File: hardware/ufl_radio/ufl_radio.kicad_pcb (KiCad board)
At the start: 6 copper layers, 46.8 x 62 mm, 142 parts, among them J2 U.FL, J3 Shield, J4 Shield, J5 U.FL, J6 Shield, J7 U.FL, J8 Shield, J9 U.FL, U1 MAX2769B, U2 CS48520S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

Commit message: Nearly ready
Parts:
- moved C37 14.7 mm to (175.8, 93.5)
- moved C42 14.7 mm to (188.8, 85.0)
- moved C22 10.3 mm to (188.8, 115.5), turned to 90 degrees
- moved C48 10.3 mm to (178.6, 86.8), turned to -90 degrees
- moved C16 8.96 mm to (178.6, 117.2), turned to -90 degrees
- moved C51 8.96 mm to (179.0, 77.8), turned to 0 degrees
- moved C39 8.73 mm to (184.2, 95.5), turned to 0 degrees
- moved C24 8.02 mm to (179.6, 117.2), turned to -90 degrees
- moved C54 7.33 mm to (184.2, 109.8), turned to 0 degrees
- moved C57 7.33 mm to (188.8, 100.3), turned to 90 degrees
- moved C18 5.45 mm to (179.0, 108.3)
- moved C27 5.31 mm to (184.0, 114.3), turned to 0 degrees
- moved C40 5.31 mm to (179.6, 86.8), turned to -90 degrees
- moved C49 5.31 mm to (184.0, 83.8), turned to 0 degrees
- moved C28 4.61 mm to (184.2, 94.5)
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
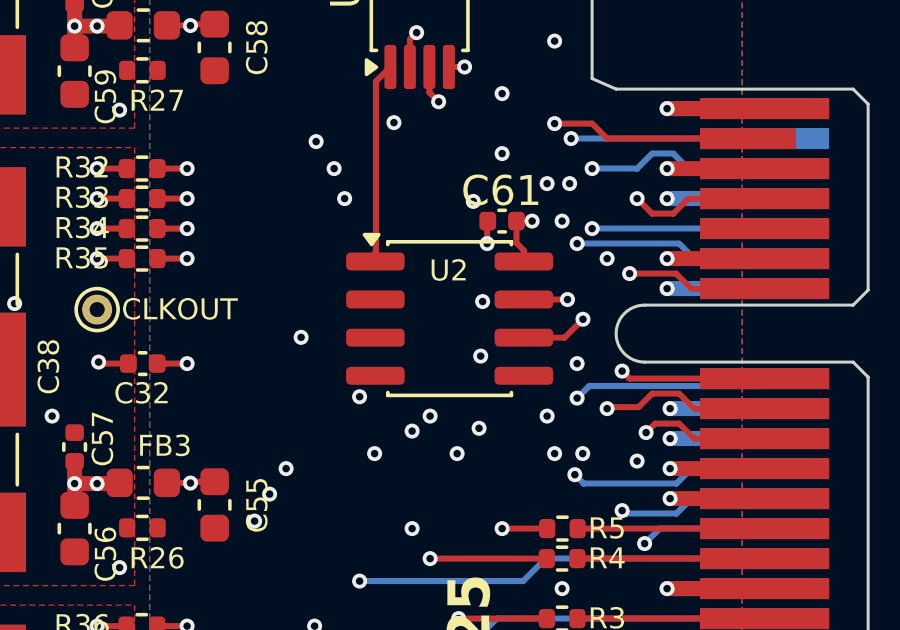
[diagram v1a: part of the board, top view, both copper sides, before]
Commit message: Replace the RS485 driver as it is no longer in production
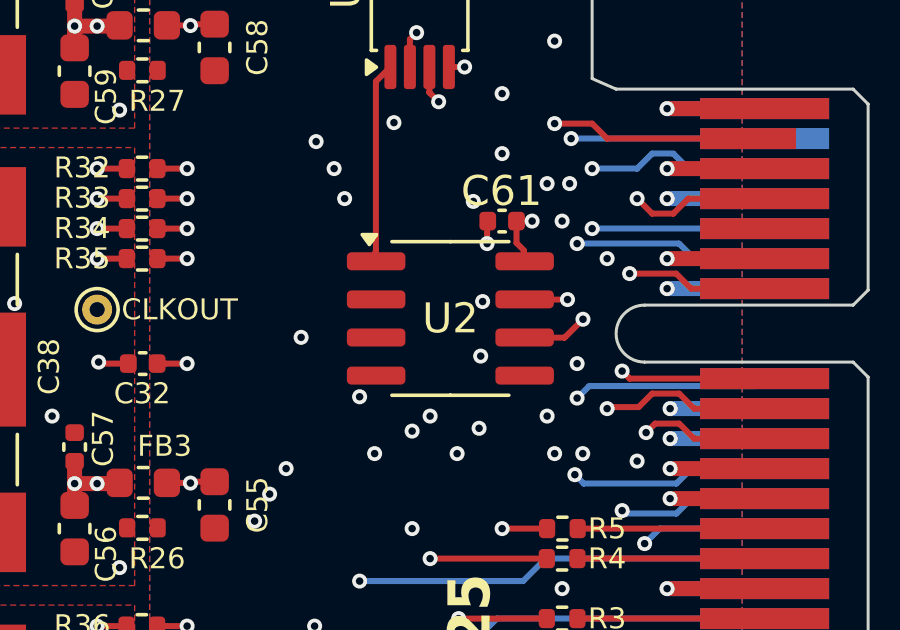
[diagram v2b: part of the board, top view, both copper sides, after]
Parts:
- U2: value CS48520S -> CS48520AS

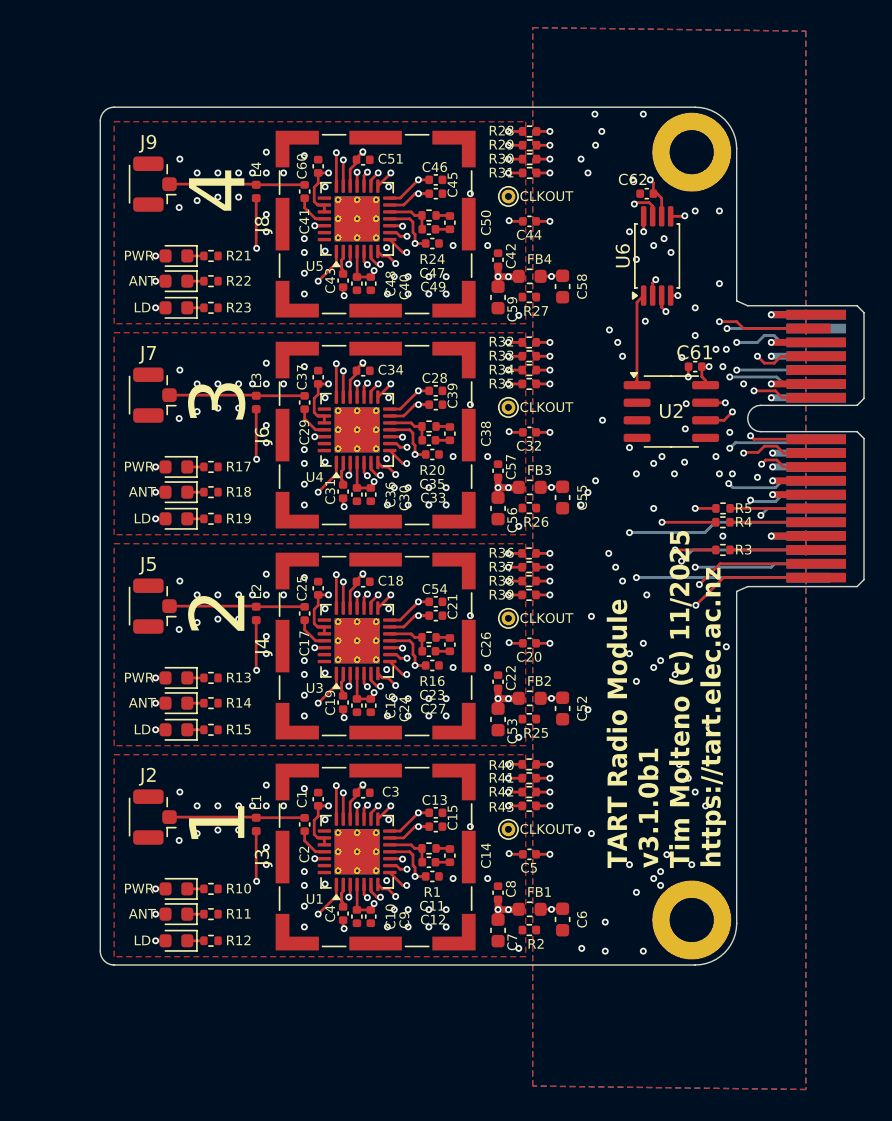
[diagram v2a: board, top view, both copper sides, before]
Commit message: Add a better panelize script and get the impedance right
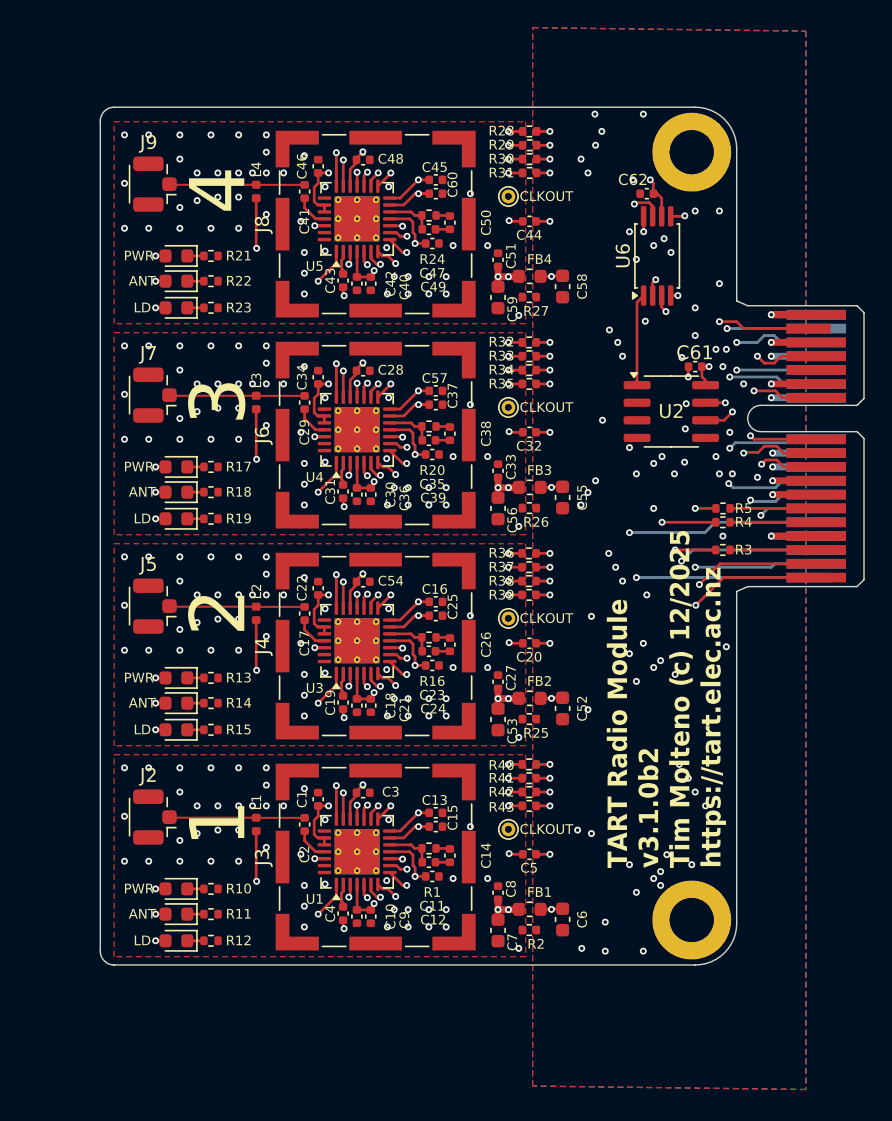
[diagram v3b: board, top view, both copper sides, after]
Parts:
- moved C22 14.7 mm to (175.8, 108.8)
- moved C51 12.1 mm to (188.8, 85.0), turned to 90 degrees
- moved C42 10.3 mm to (178.6, 86.8), turned to -90 degrees
- moved C16 9.42 mm to (184.2, 109.8), turned to 0 degrees
- moved C18 8.96 mm to (178.6, 117.2), turned to -90 degrees
- moved C48 8.96 mm to (179.0, 77.8), turned to 0 degrees
- moved C25 8.73 mm to (184.2, 110.8), turned to 0 degrees
- moved C37 8.73 mm to (184.2, 95.5), turned to 0 degrees
- moved C60 8.73 mm to (184.2, 80.2), turned to 0 degrees
- moved C46 8.56 mm to (175.8, 78.3), turned to 90 degrees
- moved C21 8.02 mm to (179.6, 117.2), turned to -90 degrees
- moved C57 7.33 mm to (184.2, 94.5), turned to 0 degrees
- moved C28 5.45 mm to (179.0, 93.0)
- moved C54 5.45 mm to (179.0, 108.3)
- moved C24 5.31 mm to (184.0, 114.3), turned to 0 degrees
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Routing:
- net /Radio4/AGND_local: vias 35 -> 46
- net /Radio3/AGND_local: vias 35 -> 46
- net /Radio2/AGND_local: vias 35 -> 46
- net /Radio1/AGND_local: vias 35 -> 46
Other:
- board text added: "TART Radio Module v3.1.0b2 Tim Molteno (c) 12/2025 https://tart.elec.ac.nz"
- board text added: "TART Radio Telescope Radio Module v3.1.0b2 Tim Molteno (c) 12/2025 https://tart.elec.ac.nz"
- board text removed: "TART Radio Module v3.1.0b1 Tim Molteno (c) 11/2025 https://tart.elec.ac.nz"
- board text removed: "TART Radio Telescope Radio Module v3.1.0b1 Tim Molteno (c) 11/2025 https://tart.elec.ac.nz"

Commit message: Fix up ground rules
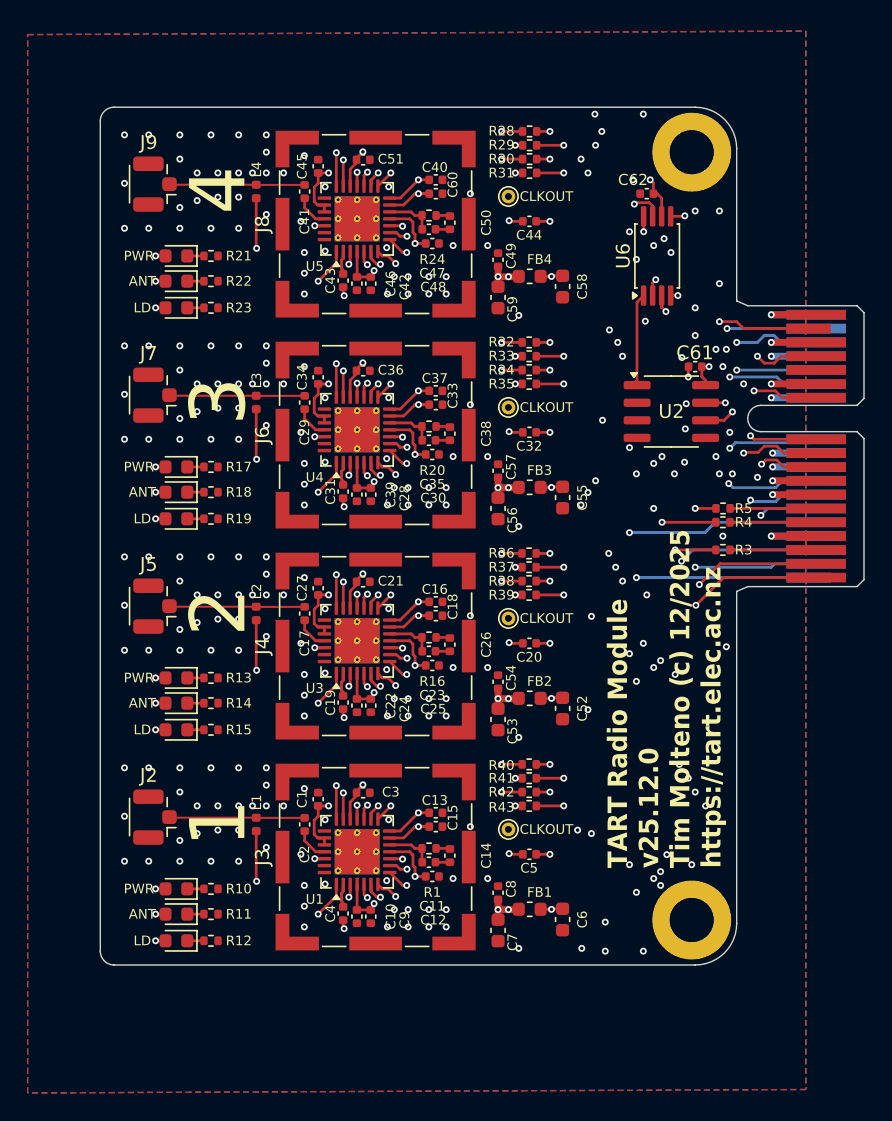
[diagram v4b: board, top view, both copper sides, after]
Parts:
- removed R2, R25, R26, R27: 0, Resistor_SMD:R_0402_1005Metric
- moved C27 14.7 mm to (175.8, 108.8)
- moved C51 12.1 mm to (179.0, 77.8), turned to 0 degrees
- moved C54 12.1 mm to (188.8, 115.5), turned to 90 degrees
- moved C21 8.97 mm to (179.0, 108.3), turned to 0 degrees
- moved C28 8.97 mm to (179.6, 102.0), turned to -90 degrees
- moved C36 8.97 mm to (179.0, 93.0), turned to 0 degrees
- moved C22 8.93 mm to (178.6, 117.2), turned to -90 degrees
- moved C46 8.93 mm to (178.6, 86.8), turned to -90 degrees
- moved C40 8.85 mm to (184.2, 79.2), turned to 0 degrees
- moved C18 8.65 mm to (184.2, 110.8), turned to 0 degrees
- moved C45 8.56 mm to (175.8, 78.3), turned to 90 degrees
- moved C48 7.85 mm to (184.0, 83.8)
- moved C57 7.33 mm to (188.8, 100.3), turned to 90 degrees
- moved C33 6.56 mm to (184.2, 95.5), turned to 0 degrees
- moved C30 6.17 mm to (184.0, 99.1), turned to 0 degrees
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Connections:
- C1 pad 2: /Radio1/AGND_local -> GNDREF
- C10 pad 2: /Radio1/AGND_local -> GNDREF
- C11 pad 1: /Radio1/AGND_local -> GNDREF
- C12 pad 2: /Radio1/AGND_local -> GNDREF
- C13 pad 2: /Radio1/AGND_local -> GNDREF
- C14 pad 2: /Radio1/AGND_local -> GNDREF
- C15 pad 2: /Radio1/AGND_local -> GNDREF
- C16 pad 2: /Radio2/AGND_local -> GNDREF
- C18 pad 2: /Radio2/AGND_local -> GNDREF
- C21 pad 2: /Radio2/AGND_local -> GNDREF
- C22 pad 2: /Radio2/AGND_local -> GNDREF
- C23 pad 1: /Radio2/AGND_local -> GNDREF
- C24 pad 2: /Radio2/AGND_local -> GNDREF
- C25 pad 2: /Radio2/AGND_local -> GNDREF
- C26 pad 2: /Radio2/AGND_local -> GNDREF
- C27 pad 2: /Radio2/AGND_local -> GNDREF
- C28 pad 2: /Radio3/AGND_local -> GNDREF
- C3 pad 2: /Radio1/AGND_local -> GNDREF
- C30 pad 2: /Radio3/AGND_local -> GNDREF
- C33 pad 2: /Radio3/AGND_local -> GNDREF
- C34 pad 2: /Radio3/AGND_local -> GNDREF
- C35 pad 1: /Radio3/AGND_local -> GNDREF
- C36 pad 2: /Radio3/AGND_local -> GNDREF
- C37 pad 2: /Radio3/AGND_local -> GNDREF
- C38 pad 2: /Radio3/AGND_local -> GNDREF
- C39 pad 2: /Radio3/AGND_local -> GNDREF
- C40 pad 2: /Radio4/AGND_local -> GNDREF
- C42 pad 2: /Radio4/AGND_local -> GNDREF
- C45 pad 2: /Radio4/AGND_local -> GNDREF
- C46 pad 2: /Radio4/AGND_local -> GNDREF
- C47 pad 1: /Radio4/AGND_local -> GNDREF
- C48 pad 2: /Radio4/AGND_local -> GNDREF
- C49 pad 2: /Radio4/AGND_local -> GNDREF
- C50 pad 2: /Radio4/AGND_local -> GNDREF
- C51 pad 2: /Radio4/AGND_local -> GNDREF
- C53 pad 2: /Radio2/AGND_local -> GNDREF
- C54 pad 2: /Radio2/AGND_local -> GNDREF
- C56 pad 2: /Radio3/AGND_local -> GNDREF
- C57 pad 2: /Radio3/AGND_local -> GNDREF
- C59 pad 2: /Radio4/AGND_local -> GNDREF
- C60 pad 2: /Radio4/AGND_local -> GNDREF
- C7 pad 2: /Radio1/AGND_local -> GNDREF
- C8 pad 2: /Radio1/AGND_local -> GNDREF
- C9 pad 2: /Radio1/AGND_local -> GNDREF
- J2 pad 2: /Radio1/AGND_local -> GNDREF
- J3 pad 1: /Radio1/AGND_local -> GNDREF
- J4 pad 1: /Radio2/AGND_local -> GNDREF
- J5 pad 2: /Radio2/AGND_local -> GNDREF
- J6 pad 1: /Radio3/AGND_local -> GNDREF
- J7 pad 2: /Radio3/AGND_local -> GNDREF
- J8 pad 1: /Radio4/AGND_local -> GNDREF
- J9 pad 2: /Radio4/AGND_local -> GNDREF
- R10 pad 2: /Radio1/AGND_local -> GNDREF
- R11 pad 2: /Radio1/AGND_local -> GNDREF
- R12 pad 2: /Radio1/AGND_local -> GNDREF
- R13 pad 2: /Radio2/AGND_local -> GNDREF
- R14 pad 2: /Radio2/AGND_local -> GNDREF
- R15 pad 2: /Radio2/AGND_local -> GNDREF
- R17 pad 2: /Radio3/AGND_local -> GNDREF
- R18 pad 2: /Radio3/AGND_local -> GNDREF
- R19 pad 2: /Radio3/AGND_local -> GNDREF
- R21 pad 2: /Radio4/AGND_local -> GNDREF
- R22 pad 2: /Radio4/AGND_local -> GNDREF
- R23 pad 2: /Radio4/AGND_local -> GNDREF
- U1 pad 29: /Radio1/AGND_local -> GNDREF
- U3 pad 29: /Radio2/AGND_local -> GNDREF
- U4 pad 29: /Radio3/AGND_local -> GNDREF
- U5 pad 29: /Radio4/AGND_local -> GNDREF
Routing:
- net GNDREF: track 30.4 -> 34.6 mm, vias 35 -> 219
- net /Radio4/AGND_local: track 1.04 -> 0.00 mm, vias 46 -> 0
- net /Radio3/AGND_local: track 1.04 -> 0.00 mm, vias 46 -> 0
- net /Radio2/AGND_local: track 1.04 -> 0.00 mm, vias 46 -> 0
- net /Radio1/AGND_local: track 1.04 -> 0.00 mm, vias 46 -> 0
- added copper zone on In2.Cu, net GNDREF
- added copper zone on In4.Cu, net GNDREF
- removed copper zone on F.Cu, net /Radio1/AGND_local
- removed copper zone on In1.Cu, net /Radio1/AGND_local
- removed copper zone on F.Cu, net /Radio2/AGND_local
- removed copper zone on In1.Cu, net /Radio2/AGND_local
- removed copper zone on F.Cu, net /Radio3/AGND_local
- removed copper zone on In1.Cu, net /Radio3/AGND_local
- removed copper zone on F.Cu, net /Radio4/AGND_local
- removed copper zone on In1.Cu, net /Radio4/AGND_local
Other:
- board text added: "TART Radio Module v25.12.0 Tim Molteno (c) 12/2025 https://tart.elec.ac.nz"
- board text removed: "TART Radio Module v3.1.0b2 Tim Molteno (c) 12/2025 https://tart.elec.ac.nz"

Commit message: Update and improve noise on ufl radio
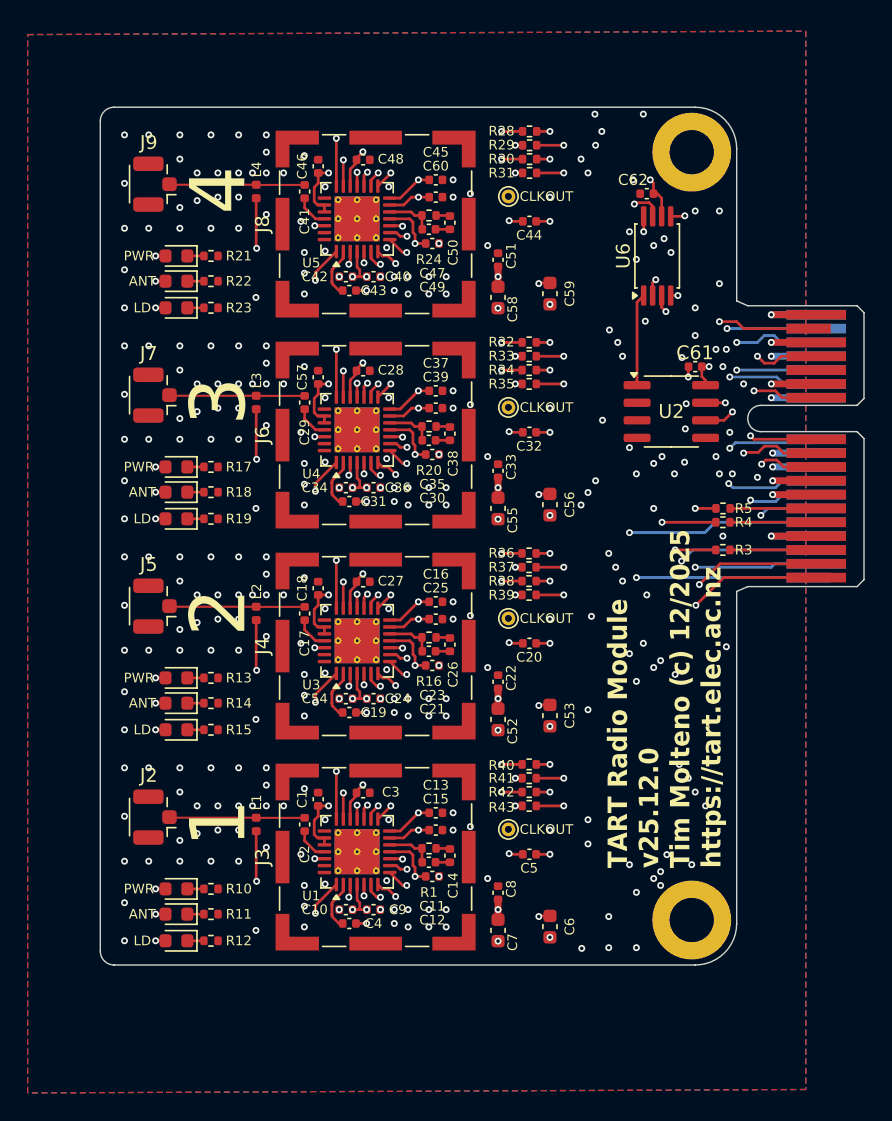
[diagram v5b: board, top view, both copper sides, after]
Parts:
- removed FB1, FB2, FB3, FB4: GZ1608D601TF, Inductor_SMD:L_0603_1608Metric
- moved C57 14.7 mm to (175.8, 93.5)
- moved C51 12.1 mm to (188.8, 85.0), turned to 90 degrees
- moved C54 11.1 mm to (177.8, 116.8), turned to 180 degrees
- moved C22 10.3 mm to (188.8, 115.5), turned to 90 degrees
- moved C28 8.97 mm to (179.0, 93.0), turned to 0 degrees
- moved C46 8.93 mm to (175.8, 78.3), turned to 90 degrees
- moved C18 8.73 mm to (175.8, 108.8), turned to 90 degrees
- moved C45 8.56 mm to (184.2, 79.2), turned to 0 degrees
- moved C36 8.48 mm to (179.8, 101.5)
- moved C39 8.46 mm to (184.2, 95.8), turned to 0 degrees
- moved C40 8.32 mm to (179.8, 86.2)
- moved C34 8.23 mm to (177.8, 101.5), turned to 180 degrees
- moved C21 7.85 mm to (184.0, 114.3)
- moved C48 7.85 mm to (179.0, 77.8)
- moved C33 6.56 mm to (188.8, 100.3), turned to 90 degrees
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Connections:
- C1 pad 1: /Radio1/3v3_local -> VCC
- C10 pad 1: /Radio1/3v3_local -> VCC
- C12 pad 1: /Radio1/3v3_local -> VCC
- C13 pad 1: /Radio1/3v3_local -> VCC
- C15 pad 1: /Radio1/3v3_local -> VCC
- C16 pad 1: /Radio2/3v3_local -> VCC
- C18 pad 1: /Radio2/3v3_local -> VCC
- C21 pad 1: /Radio2/3v3_local -> VCC
- C22 pad 1: /Radio2/3v3_local -> VCC
- C24 pad 1: /Radio2/3v3_local -> VCC
- C25 pad 1: /Radio2/3v3_local -> VCC
- C27 pad 1: /Radio2/3v3_local -> VCC
- C28 pad 1: /Radio3/3v3_local -> VCC
- C3 pad 1: /Radio1/3v3_local -> VCC
- C30 pad 1: /Radio3/3v3_local -> VCC
- C33 pad 1: /Radio3/3v3_local -> VCC
- C34 pad 1: /Radio3/3v3_local -> VCC
- C36 pad 1: /Radio3/3v3_local -> VCC
- C37 pad 1: /Radio3/3v3_local -> VCC
- C39 pad 1: /Radio3/3v3_local -> VCC
- C40 pad 1: /Radio4/3v3_local -> VCC
- C42 pad 1: /Radio4/3v3_local -> VCC
- C45 pad 1: /Radio4/3v3_local -> VCC
- C46 pad 1: /Radio4/3v3_local -> VCC
- C48 pad 1: /Radio4/3v3_local -> VCC
- C49 pad 1: /Radio4/3v3_local -> VCC
- C51 pad 1: /Radio4/3v3_local -> VCC
- C53 pad 1: /Radio2/3v3_local -> VCC
- C54 pad 1: /Radio2/3v3_local -> VCC
- C56 pad 1: /Radio3/3v3_local -> VCC
- C57 pad 1: /Radio3/3v3_local -> VCC
- C59 pad 1: /Radio4/3v3_local -> VCC
- C60 pad 1: /Radio4/3v3_local -> VCC
- C7 pad 1: /Radio1/3v3_local -> VCC
- C8 pad 1: /Radio1/3v3_local -> VCC
- C9 pad 1: /Radio1/3v3_local -> VCC
- D1 pad 2: /Radio1/3v3_local -> VCC
- D10 pad 2: /Radio4/3v3_local -> VCC
- D4 pad 2: /Radio2/3v3_local -> VCC
- D7 pad 2: /Radio3/3v3_local -> VCC
- U1 pad 11: /Radio1/3v3_local -> VCC
- U1 pad 13: /Radio1/3v3_local -> VCC
- U1 pad 14: /Radio1/3v3_local -> VCC
- U1 pad 19: /Radio1/3v3_local -> VCC
- U1 pad 23: /Radio1/3v3_local -> VCC
- U1 pad 24: /Radio1/3v3_local -> VCC
- U1 pad 4: /Radio1/3v3_local -> VCC
- U3 pad 11: /Radio2/3v3_local -> VCC
- U3 pad 13: /Radio2/3v3_local -> VCC
- U3 pad 14: /Radio2/3v3_local -> VCC
- U3 pad 19: /Radio2/3v3_local -> VCC
- U3 pad 23: /Radio2/3v3_local -> VCC
- U3 pad 24: /Radio2/3v3_local -> VCC
- U3 pad 4: /Radio2/3v3_local -> VCC
- U4 pad 11: /Radio3/3v3_local -> VCC
- U4 pad 13: /Radio3/3v3_local -> VCC
- U4 pad 14: /Radio3/3v3_local -> VCC
- U4 pad 19: /Radio3/3v3_local -> VCC
- U4 pad 23: /Radio3/3v3_local -> VCC
- U4 pad 24: /Radio3/3v3_local -> VCC
- U4 pad 4: /Radio3/3v3_local -> VCC
- U5 pad 11: /Radio4/3v3_local -> VCC
- U5 pad 13: /Radio4/3v3_local -> VCC
- U5 pad 14: /Radio4/3v3_local -> VCC
- U5 pad 19: /Radio4/3v3_local -> VCC
- U5 pad 23: /Radio4/3v3_local -> VCC
- U5 pad 24: /Radio4/3v3_local -> VCC
- U5 pad 4: /Radio4/3v3_local -> VCC
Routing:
- net VCC: track 22.2 -> 110.6 mm, vias 10 -> 46
- net /Radio4/3v3_local: track 25.8 -> 0.00 mm, vias 9 -> 0
- net /Radio2/3v3_local: track 25.8 -> 0.00 mm, vias 9 -> 0
- net /Radio1/3v3_local: track 25.8 -> 0.00 mm, vias 9 -> 0
- net /Radio3/3v3_local: track 25.8 -> 0.00 mm, vias 9 -> 0
- net Net-(U5-LNAOUT): track 1.72 -> 3.64 mm
- net Net-(U4-LNAOUT): track 1.72 -> 3.64 mm
- net Net-(U3-LNAOUT): track 1.72 -> 3.64 mm
- net Net-(U1-LNAOUT): track 1.72 -> 3.64 mm
- net /Radio1/LD: track 20.7 -> 21.7 mm
- net /Radio3/LD: track 20.7 -> 21.7 mm
- net /Radio4/LD: track 20.7 -> 21.7 mm
- net /Radio2/LD: track 20.7 -> 21.7 mm
- net /Radio4/I1: track 16.5 -> 17.1 mm
- net /Radio3/I1: track 16.5 -> 17.1 mm
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- removed copper zone on In4.Cu, net /Radio1/3v3_local
- removed copper zone on In4.Cu, net /Radio2/3v3_local
- removed copper zone on In4.Cu, net /Radio3/3v3_local
- removed copper zone on In4.Cu, net /Radio4/3v3_local
